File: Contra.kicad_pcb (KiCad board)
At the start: 2 copper layers, 231 x 76.2 mm, 125 parts, among them P1 Pad, P2 Pad, P3 Pad, P4 Pad, SW1 SW_PUSH, U1 ProMicro

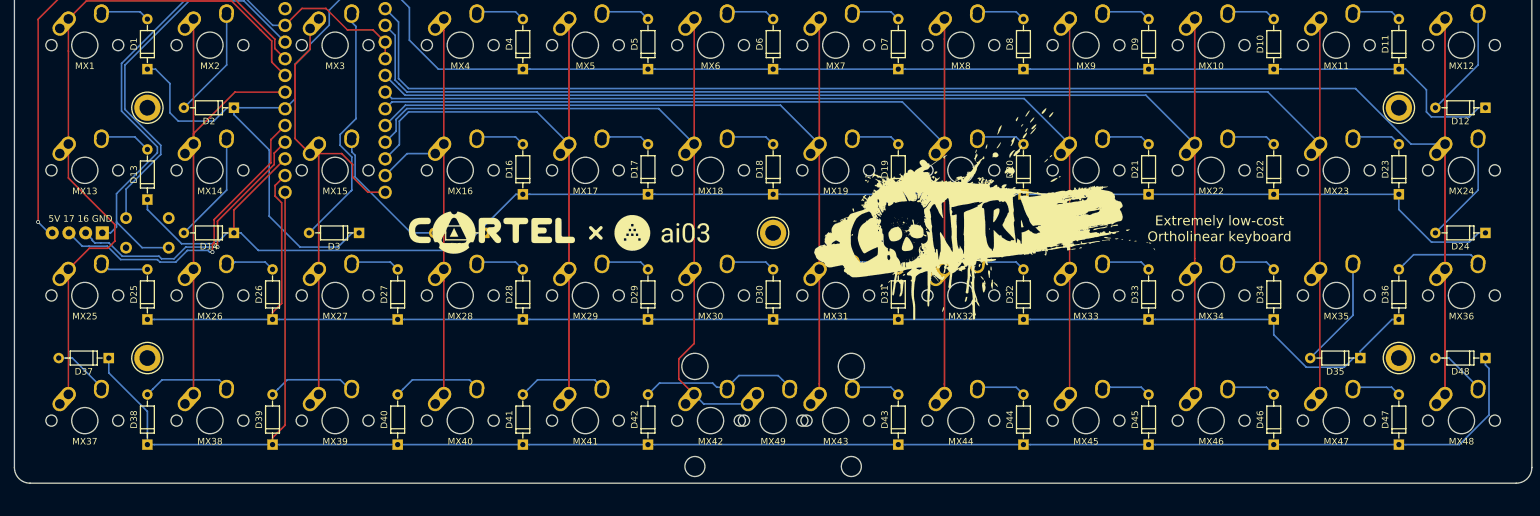
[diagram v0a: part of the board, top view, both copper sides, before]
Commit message: Fix issues present in R1
- Diode silkscreen conflict fixed
- Fix pinout on RGB breakout
- Update footprints to Rev2
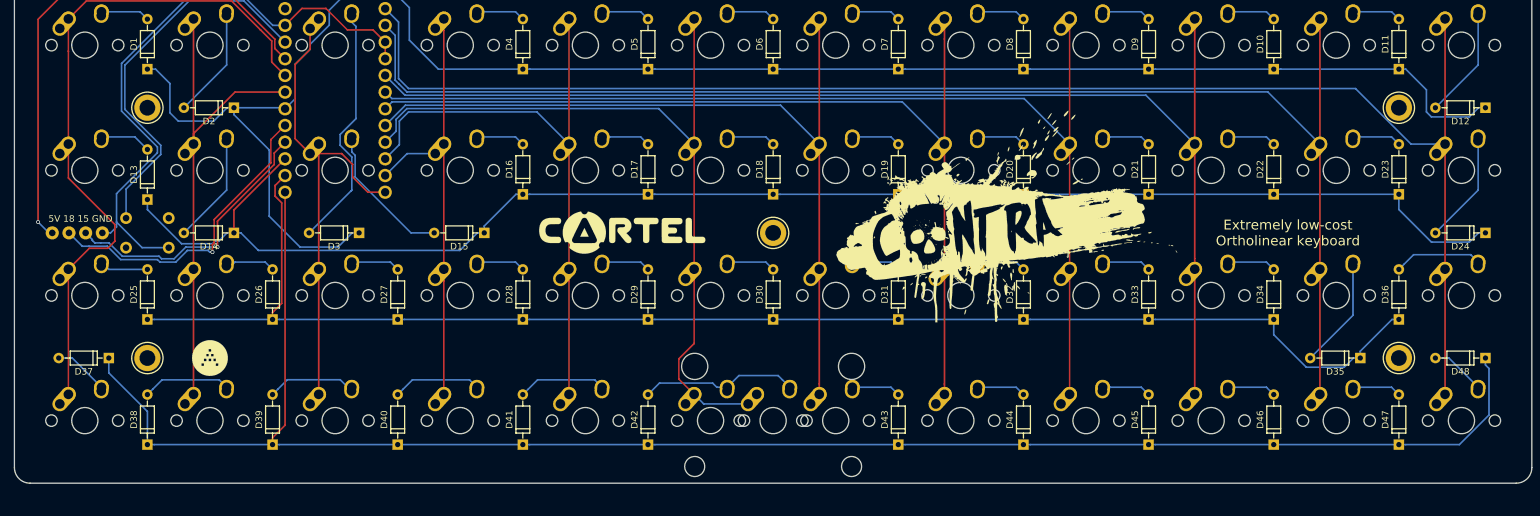
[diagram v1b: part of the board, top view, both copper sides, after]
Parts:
- removed the G*** at (127.8, 66.7)
- added G***: LOGO, ai03-logo:AI03-Silkscreen-5.4mm, F.Cu at (57.1, 85.7)
- moved G*** 19.8 mm to (119.9, 66.7)
- moved G*** 3.39 mm to (178.4, 64.1)
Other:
- board text added: "5V 18 15 GND"
- board text added: "Pro Micro here! Component side faces away from the PCB. Rev 1.6"
- board text removed: "5V 17 16 GND"
- board text removed: "Pro Micro here! Component side faces away from the PCB. Rev 1.5"
